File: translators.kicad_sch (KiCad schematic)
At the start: 66 parts

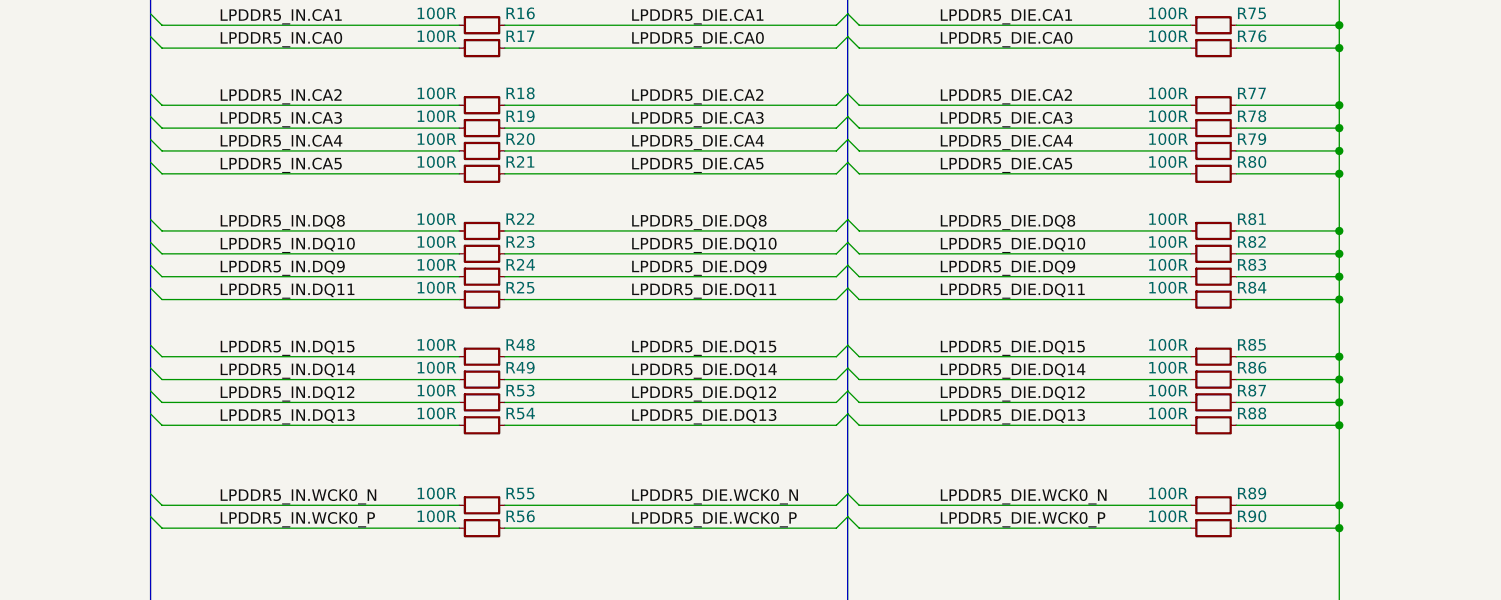
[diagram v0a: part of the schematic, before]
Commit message: [#52974] pcb: poc route using resistor arrays back
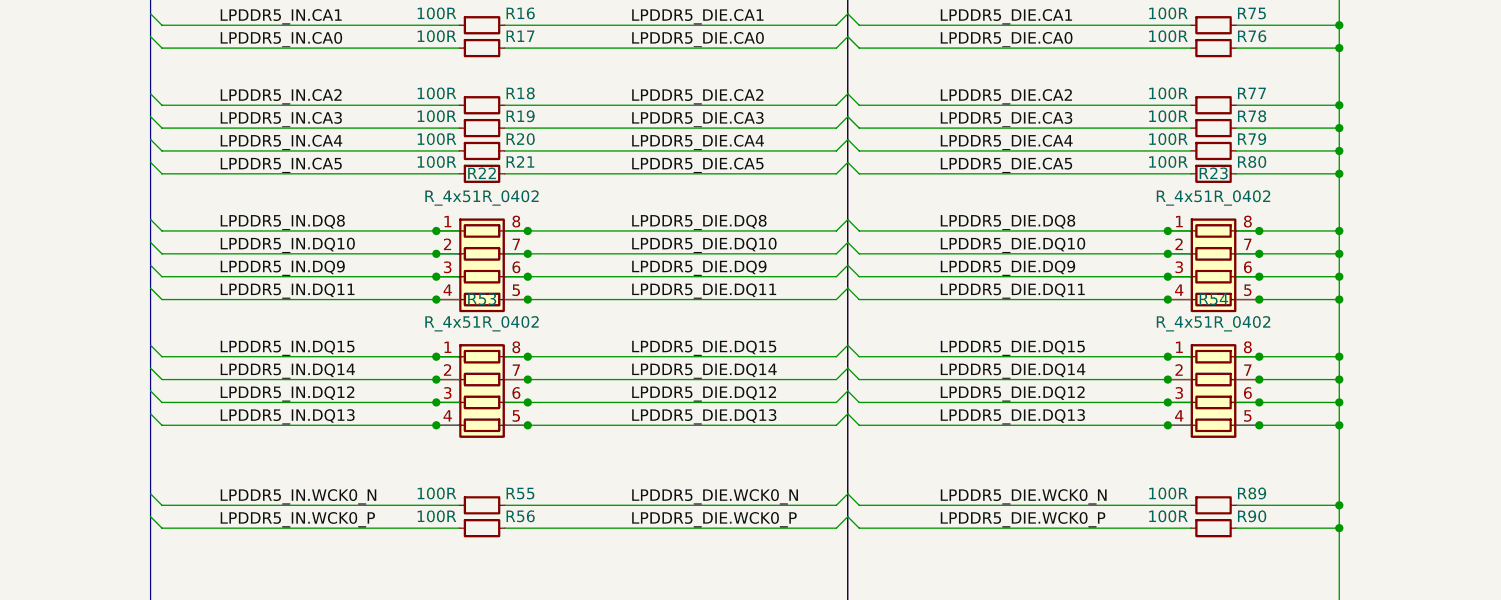
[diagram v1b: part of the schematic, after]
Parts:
- removed R22, R23, R24, R25, R48, R49, R53, R54, R81, R82, R83, R84, R85, R86, R87, R88: R_100R_0402, antmicro-footprints:R_0402_1005Metric, symbol antmicroResistors0402:R_100R_0402
- added R22, R23, R53, R54: R_4x51R_0402_array, antmicro-footprints:R_Array_4x0402, symbol antmicroResistorNetworksArrays:R_4x51R_0402_array
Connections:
- net GND: now also R23.5 (R4.2), R23.6 (R3.2), R23.7 (R2.2), R23.8 (R1.2), R54.5 (R4.2), R54.6 (R3.2), R54.7 (R2.2), R54.8 (R1.2)
- net LPDDR5_DIE.DQ10: now also R22.7 (R2.2), R23.2 (R2.1)
- net LPDDR5_DIE.DQ11: now also R22.5 (R4.2), R23.4 (R4.1)
- net LPDDR5_DIE.DQ12: now also R53.6 (R3.2), R54.3 (R3.1)
- net LPDDR5_DIE.DQ13: now also R53.5 (R4.2), R54.4 (R4.1)
- net LPDDR5_DIE.DQ14: now also R53.7 (R2.2), R54.2 (R2.1)
- net LPDDR5_DIE.DQ15: now also R53.8 (R1.2), R54.1 (R1.1)
- net LPDDR5_DIE.DQ8: now also R22.8 (R1.2), R23.1 (R1.1)
- net LPDDR5_DIE.DQ9: now also R22.6 (R3.2), R23.3 (R3.1)
- net LPDDR5_IN.DQ10: now also R22.2 (R2.1)
- net LPDDR5_IN.DQ11: now also R22.4 (R4.1)
- net LPDDR5_IN.DQ12: now also R53.3 (R3.1)
- net LPDDR5_IN.DQ13: now also R53.4 (R4.1)
- net LPDDR5_IN.DQ14: now also R53.2 (R2.1)
- net LPDDR5_IN.DQ15: now also R53.1 (R1.1)
- net LPDDR5_IN.DQ8: now also R22.1 (R1.1)
- net LPDDR5_IN.DQ9: now also R22.3 (R3.1)

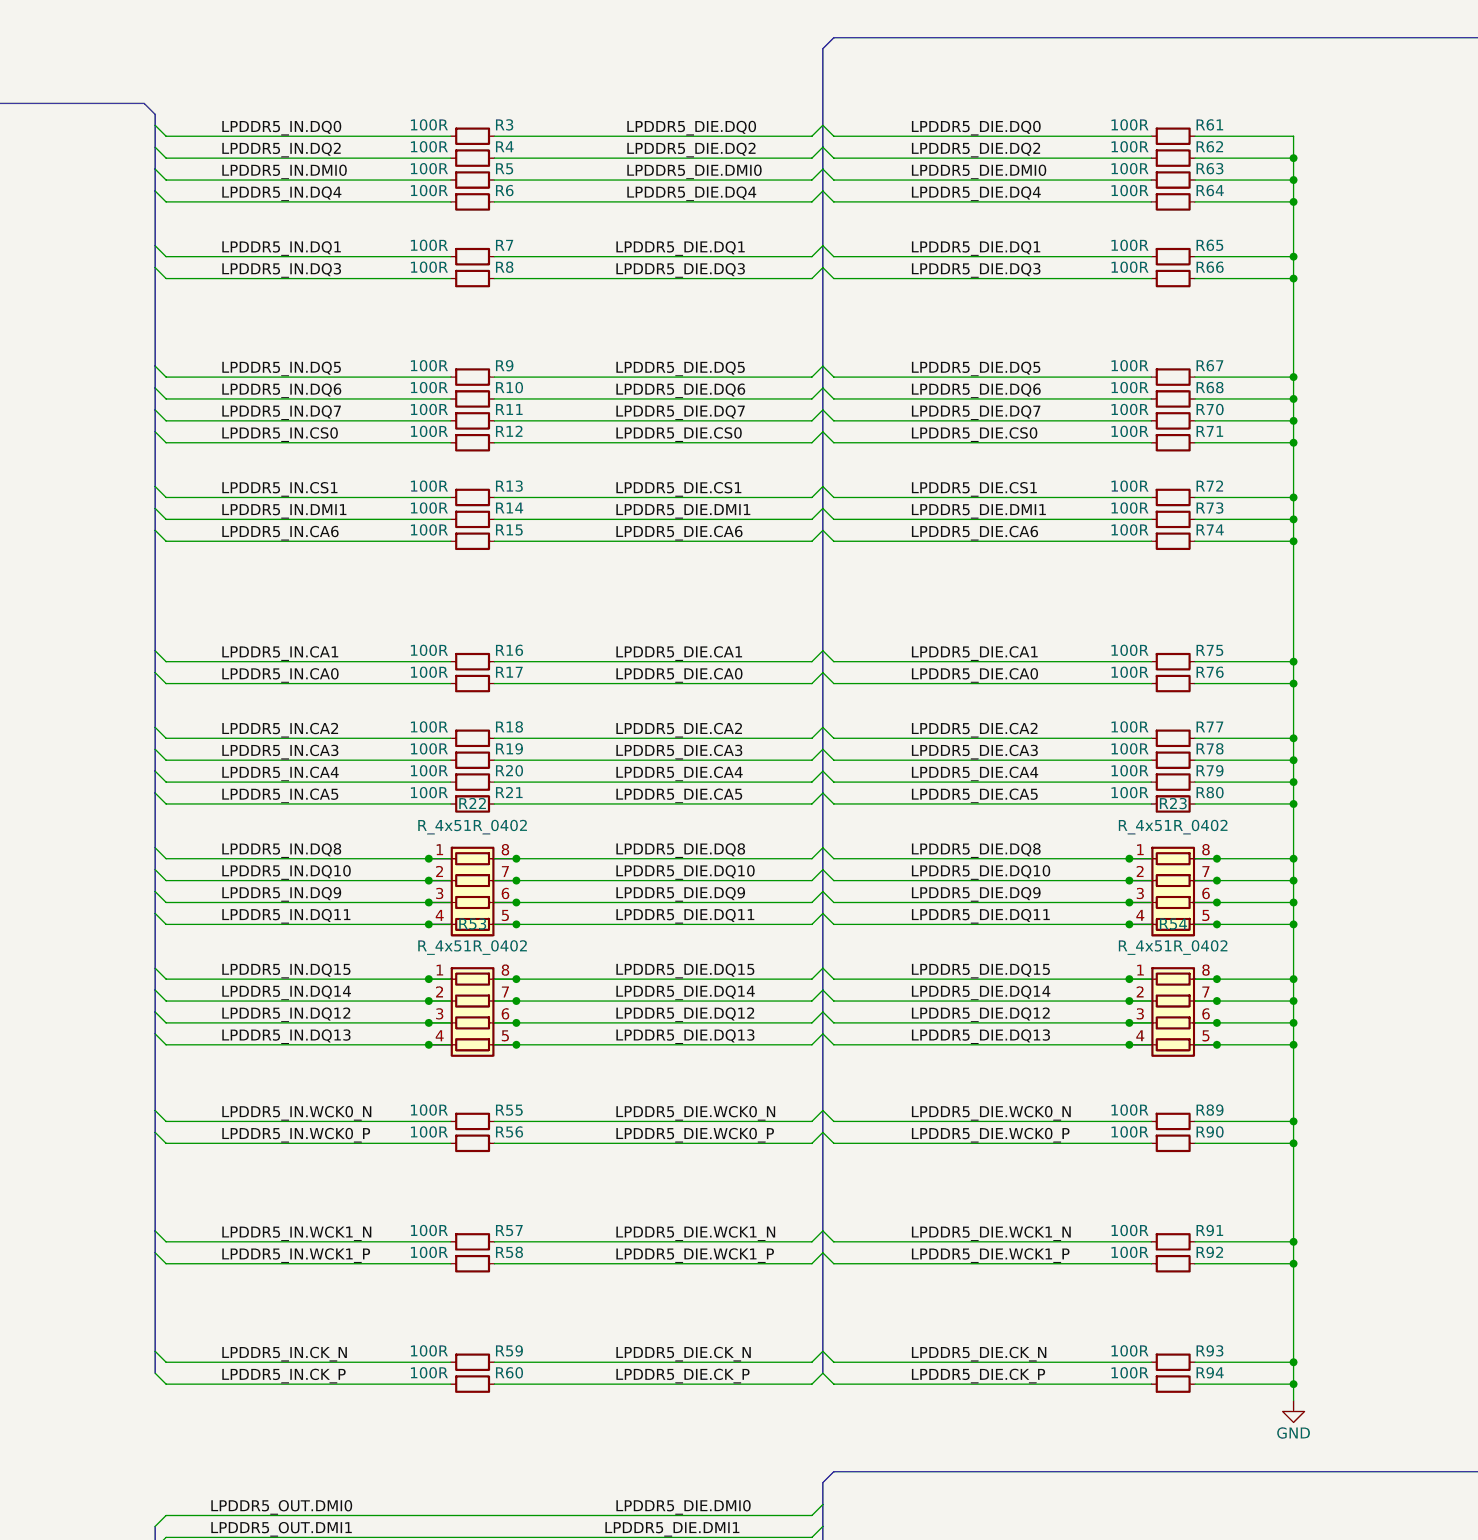
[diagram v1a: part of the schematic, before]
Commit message: [#52835] schematics: futher replacement of 0402R with resistor arrays
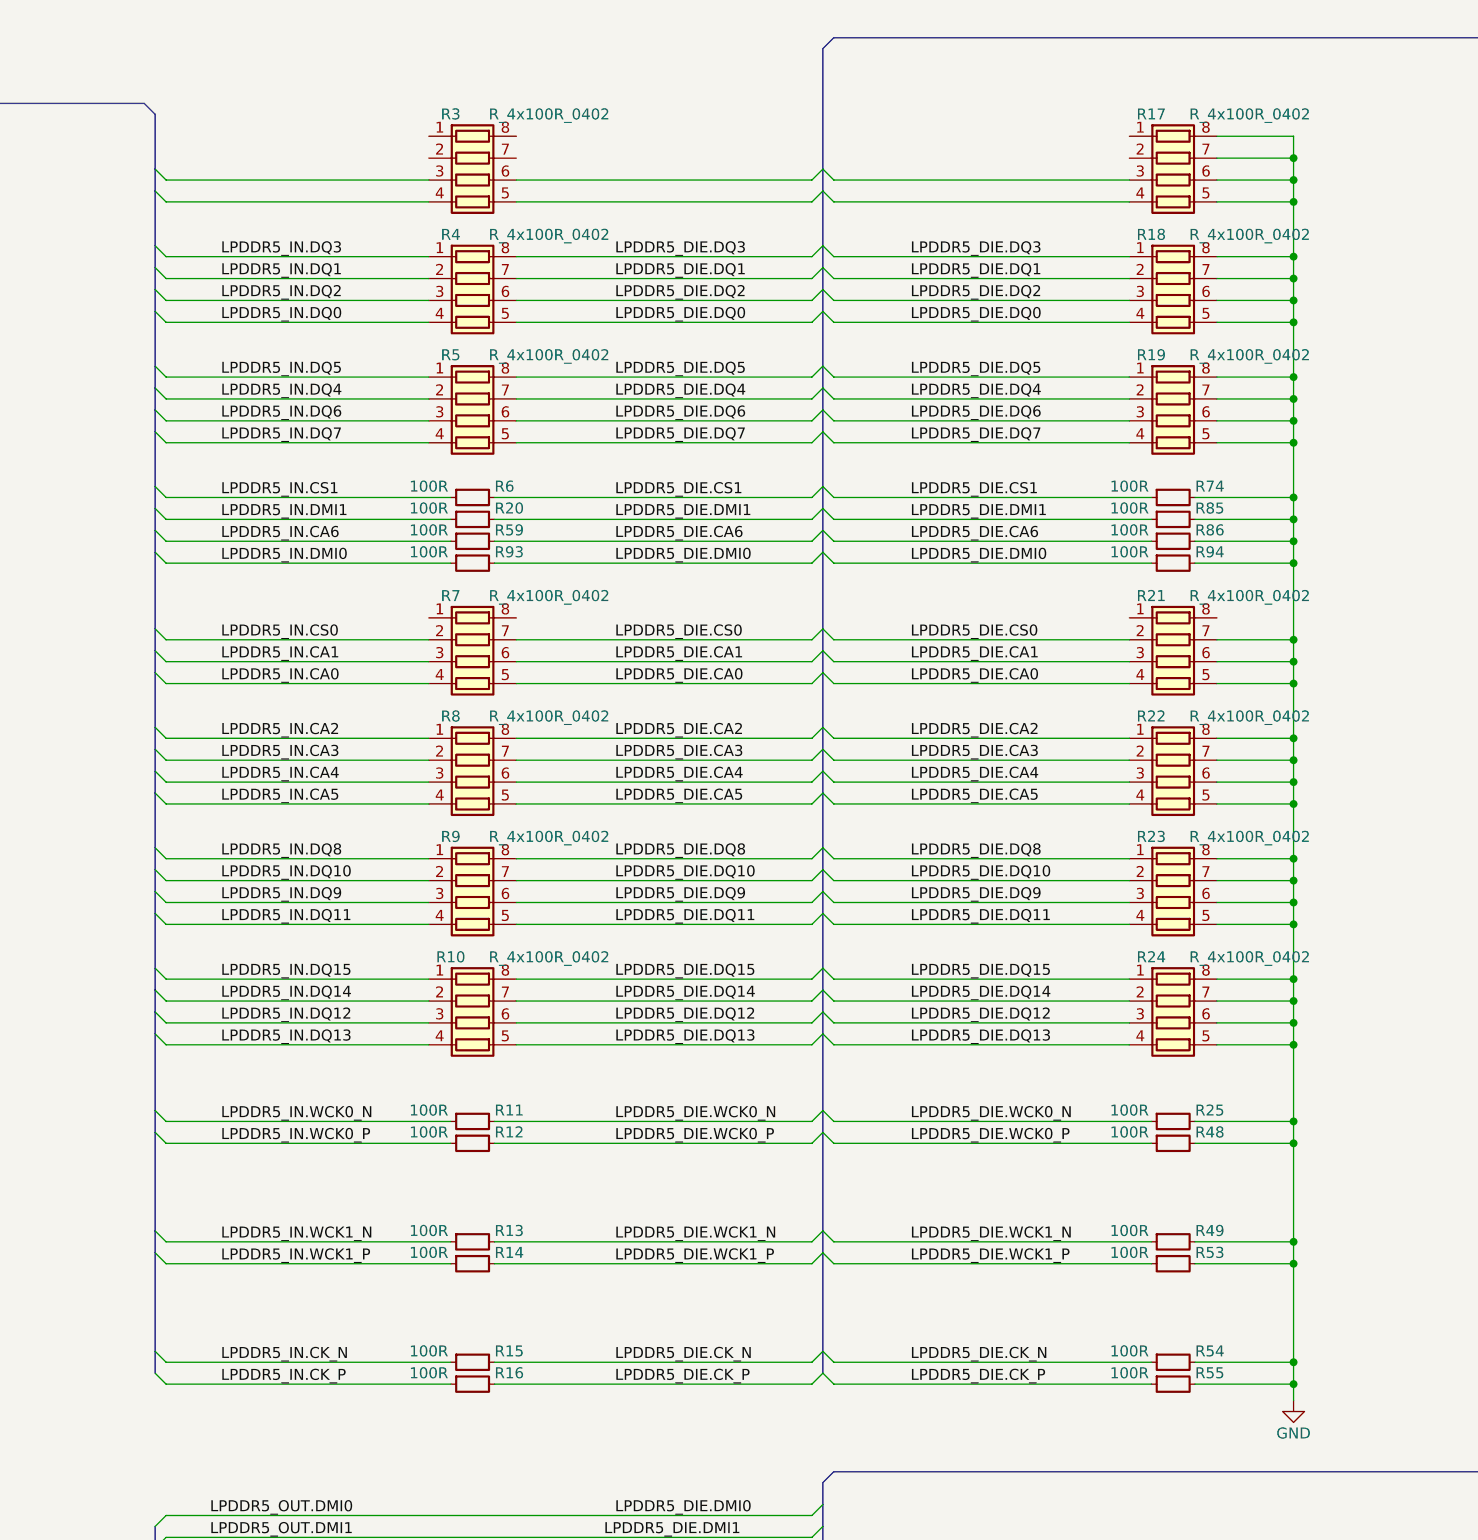
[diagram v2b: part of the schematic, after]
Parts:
- removed R10, R17, R18, R19, R21, R3, R4, R5, R56, R57, R58, R60, R61, R62, R63, R64, R65, R66, R67, R68, R7, R70, R71, R72, R73, R75, R76, R77, R78, R79, R8, R80, R89, R9, R90, R91, R92: R_100R_0402, antmicro-footprints:R_0402_1005Metric, symbol antmicroResistors0402:R_100R_0402
- removed R22, R23, R53, R54: R_4x51R_0402_array, antmicro-footprints:R_Array_4x0402, symbol antmicroResistorNetworksArrays:R_4x51R_0402_array
- added R10, R17, R18, R19, R21, R22, R23, R24, R3, R4, R5, R7, R8, R9: R_4x100R_0402_array, antmicro-footprints:R_Array_4x0402, symbol antmicroResistorNetworksArrays:R_4x100R_0402_array
- added R25, R48, R49, R53, R54, R85, R86: R_100R_0402, antmicro-footprints:R_0402_1005Metric, symbol antmicroResistors0402:R_100R_0402
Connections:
- net GND: now also R55.2, R17.5 (R4.2), R17.6 (R3.2), R17.7 (R2.2), R17.8 (R1.2), R18.5 (R4.2), R18.6 (R3.2), R18.7 (R2.2), R18.8 (R1.2), R19.5 (R4.2), R19.6 (R3.2), R19.7 (R2.2), R19.8 (R1.2), R21.5 (R4.2), R21.6 (R3.2), R21.7 (R2.2), R22.5 (R4.2), R22.6 (R3.2), R22.7 (R2.2), R22.8 (R1.2), R23.5 (R4.2), R23.6 (R3.2), R23.7 (R2.2), R23.8 (R1.2), R24.5 (R4.2), R24.6 (R3.2), R24.7 (R2.2), R24.8 (R1.2), R25.2, R48.2, R49.2, R53.2, R54.2, R85.2, R86.2; no longer R93.2
- net LPDDR5_DIE.CA0: now also R21.4 (R4.1), R7.5 (R4.2)
- net LPDDR5_DIE.CA1: now also R21.3 (R3.1), R7.6 (R3.2); no longer R16.2
- net LPDDR5_DIE.CA2: now also R22.1 (R1.1), R8.8 (R1.2)
- net LPDDR5_DIE.CA3: now also R22.2 (R2.1), R8.7 (R2.2)
- net LPDDR5_DIE.CA4: now also R22.3 (R3.1), R8.6 (R3.2); no longer R20.2
- net LPDDR5_DIE.CA5: now also R22.4 (R4.1), R8.5 (R4.2)
- net LPDDR5_DIE.CA6: now also R59.2, R86.1; no longer R15.2, R74.1
- net LPDDR5_DIE.CK_N: now also R15.2, R54.1; no longer R59.2, R93.1
- net LPDDR5_DIE.CK_P: now also R16.2, R55.1; no longer R94.1
- net LPDDR5_DIE.CS0: now also R21.2 (R2.1), R7.7 (R2.2); no longer R12.2
- net LPDDR5_DIE.CS1: now also R6.2, R74.1; no longer R13.2
- net LPDDR5_DIE.DMI0: now also R93.2, R94.1
- net LPDDR5_DIE.DMI1: now also R20.2, R85.1; no longer R14.2
- net LPDDR5_DIE.DQ0: now also R18.4 (R4.1), R4.5 (R4.2)
- net LPDDR5_DIE.DQ1: now also R18.2 (R2.1), R4.7 (R2.2)
- net LPDDR5_DIE.DQ10: now also R23.2 (R2.1), R9.7 (R2.2)
- net LPDDR5_DIE.DQ11: now also R23.4 (R4.1), R9.5 (R4.2)
- net LPDDR5_DIE.DQ12: now also R10.6 (R3.2), R24.3 (R3.1)
- net LPDDR5_DIE.DQ13: now also R10.5 (R4.2), R24.4 (R4.1)
- net LPDDR5_DIE.DQ14: now also R10.7 (R2.2), R24.2 (R2.1)
- net LPDDR5_DIE.DQ15: now also R10.8 (R1.2), R24.1 (R1.1)
- net LPDDR5_DIE.DQ2: now also R18.3 (R3.1), R4.6 (R3.2)
- net LPDDR5_DIE.DQ3: now also R18.1 (R1.1), R4.8 (R1.2)
- net LPDDR5_DIE.DQ4: now also R19.2 (R2.1), R5.7 (R2.2); no longer R6.2
- net LPDDR5_DIE.DQ5: now also R19.1 (R1.1), R5.8 (R1.2)
- net LPDDR5_DIE.DQ6: now also R19.3 (R3.1), R5.6 (R3.2)
- net LPDDR5_DIE.DQ7: now also R19.4 (R4.1), R5.5 (R4.2); no longer R11.2
- net LPDDR5_DIE.DQ8: now also R23.1 (R1.1), R9.8 (R1.2)
- net LPDDR5_DIE.DQ9: now also R23.3 (R3.1), R9.6 (R3.2)
- net LPDDR5_DIE.WCK0_N: now also R11.2, R25.1; no longer R55.2
- net LPDDR5_DIE.WCK0_P: now also R12.2, R48.1
- net LPDDR5_DIE.WCK1_N: now also R13.2, R49.1
- net LPDDR5_DIE.WCK1_P: now also R14.2, R53.1
- net LPDDR5_IN.CA0: now also R7.4 (R4.1)
- net LPDDR5_IN.CA1: now also R7.3 (R3.1); no longer R16.1
- net LPDDR5_IN.CA2: now also R8.1 (R1.1)
- net LPDDR5_IN.CA3: now also R8.2 (R2.1)
- net LPDDR5_IN.CA4: now also R8.3 (R3.1); no longer R20.1
- net LPDDR5_IN.CA5: now also R8.4 (R4.1)
- net LPDDR5_IN.CA6: now also R59.1; no longer R15.1
- net LPDDR5_IN.CK_N: now also R15.1; no longer R59.1
- net LPDDR5_IN.CK_P: now also R16.1
- net LPDDR5_IN.CS0: now also R7.2 (R2.1); no longer R12.1
- net LPDDR5_IN.CS1: now also R6.1; no longer R13.1
- net LPDDR5_IN.DMI0: now also R93.1
- net LPDDR5_IN.DMI1: now also R20.1; no longer R14.1
- net LPDDR5_IN.DQ0: now also R4.4 (R4.1)
- net LPDDR5_IN.DQ1: now also R4.2 (R2.1)
- net LPDDR5_IN.DQ10: now also R9.2 (R2.1)
- net LPDDR5_IN.DQ11: now also R9.4 (R4.1)
- net LPDDR5_IN.DQ12: now also R10.3 (R3.1)
- net LPDDR5_IN.DQ13: now also R10.4 (R4.1)
- net LPDDR5_IN.DQ14: now also R10.2 (R2.1)
- net LPDDR5_IN.DQ15: now also R10.1 (R1.1)
- net LPDDR5_IN.DQ2: now also R4.3 (R3.1)
- net LPDDR5_IN.DQ3: now also R4.1 (R1.1)
- net LPDDR5_IN.DQ4: now also R5.2 (R2.1); no longer R6.1
- net LPDDR5_IN.DQ5: now also R5.1 (R1.1)
- net LPDDR5_IN.DQ6: now also R5.3 (R3.1)
- net LPDDR5_IN.DQ7: now also R5.4 (R4.1); no longer R11.1
- net LPDDR5_IN.DQ8: now also R9.1 (R1.1)
- net LPDDR5_IN.DQ9: now also R9.3 (R3.1)
- net LPDDR5_IN.WCK0_N: now also R11.1; no longer R55.1
- net LPDDR5_IN.WCK0_P: now also R12.1
- net LPDDR5_IN.WCK1_N: now also R13.1
- net LPDDR5_IN.WCK1_P: now also R14.1
